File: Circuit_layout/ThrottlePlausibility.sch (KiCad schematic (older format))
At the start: 65 parts, among them Q2 MMBF170, SW2 TS5A3159-Q1, U18 TS912, U22 TS372, U23 TLP293, U24 TLP293, U3 MCP6004, U4 MCP6004, U5 LM7810CT, U6 TS912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

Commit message: fixing nets. most done except for GND/driving issue
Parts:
- W10, W11, W6, W7, W8: footprint (none) -> Measurement_Points:Measurement_Point_Round-SMD-Pad_Big
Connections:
- net VCC is gone; now on net +5V: U8.11 (VCC)

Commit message: current sensor enable
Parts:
- W4, W5: footprint (none) -> Measurement_Points:Measurement_Point_Round-SMD-Pad_Big

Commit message: modifying hvpl
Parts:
- U5: footprint TO-220 -> Power_Integrations:TO-220
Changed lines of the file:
@@
 LIBS:xilinx
 LIBS:Zilog
-LIBS:pacman-main-cache
 LIBS:bss84
 LIBS:+10v
@@
 F 0 "JP1" H 13700 4600 50  0000 L CNN
 F 1 "JUMPER3" H 13650 4800 50  0000 C BNN
-F 2 "" H 13650 4700 50  0000 C CNN
+F 2 "" H 13650 4700 50  0001 C CNN
 F 3 "" H 13650 4700 50  0000 C CNN
 	1    13650 4700
@@
 F 0 "U5" H 1800 4300 50  0000 C CNN
 F 1 "LM7810CT" H 2000 4300 50  0000 L CNN
-F 2 "TO-220" H 2000 4200 50  0001 C CIN
+F 2 "Power_Integrations:TO-220" H 2000 4200 50  0001 C CIN
 F 3 "https://www.fairchildsemi.com/datasheets/LM/LM7805.pdf" H 2000 4100 50  0001 C CNN
 F 4 "LM7810CT-ND" H 2000 4100 60  0001 C CNN "DigiKey P/N"
@@
 F 0 "W9" H 11550 4970 50  0000 C CNN
 F 1 "Throttle_PL" H 11550 4900 50  0000 C CNN
-F 2 "" H 11750 4700 50  0000 C CNN
+F 2 "" H 11750 4700 50  0001 C CNN
 F 3 "" H 11750 4700 50  0000 C CNN
 	1    11550 4700

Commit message: added footprint to DPDT switch, test points, DRC passes
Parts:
- renumbered U6 to U18, U18 to U6
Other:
- moved on the sheet: C45

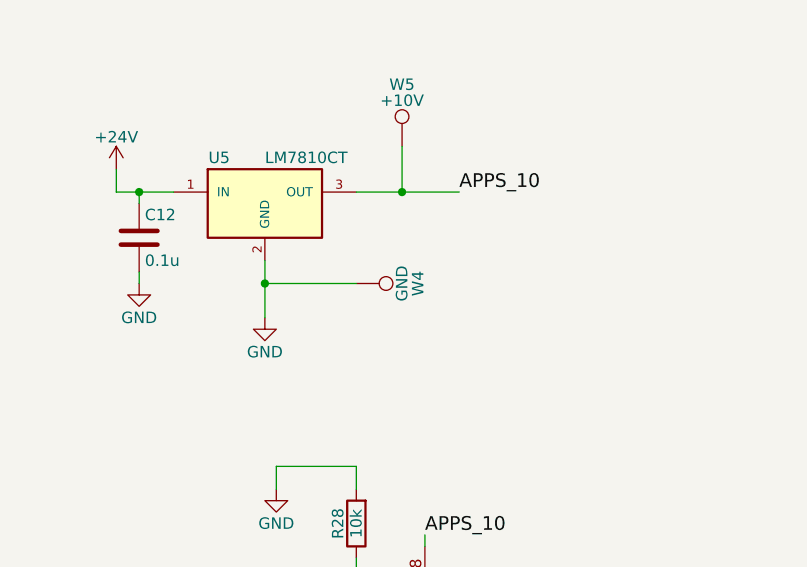
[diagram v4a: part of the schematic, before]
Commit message: cleaned up footprints of more testpoints. ran DRC again, passed
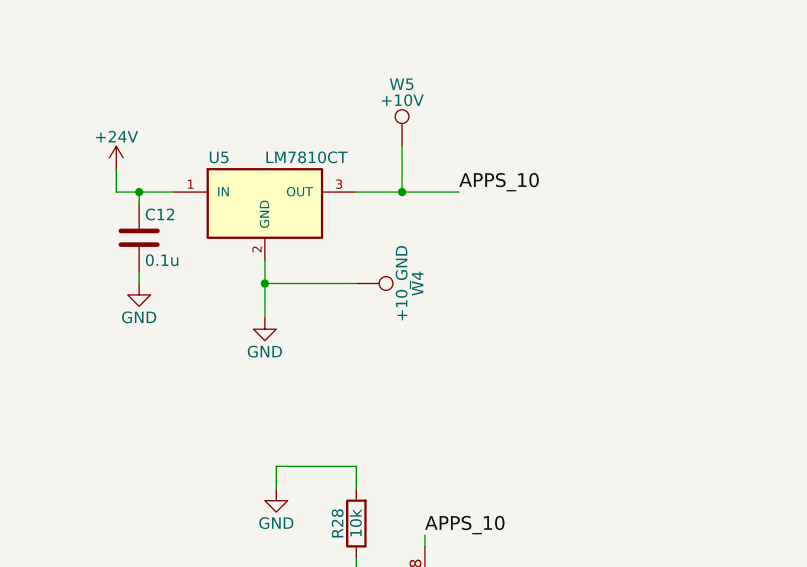
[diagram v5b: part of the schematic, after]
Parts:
- W4: value GND -> +10_GND; footprint Measurement_Points:Measurement_Point_Round-SMD-Pad_Big -> Measurement_Points:Measurement_Point_Square-SMD-Pad_Big

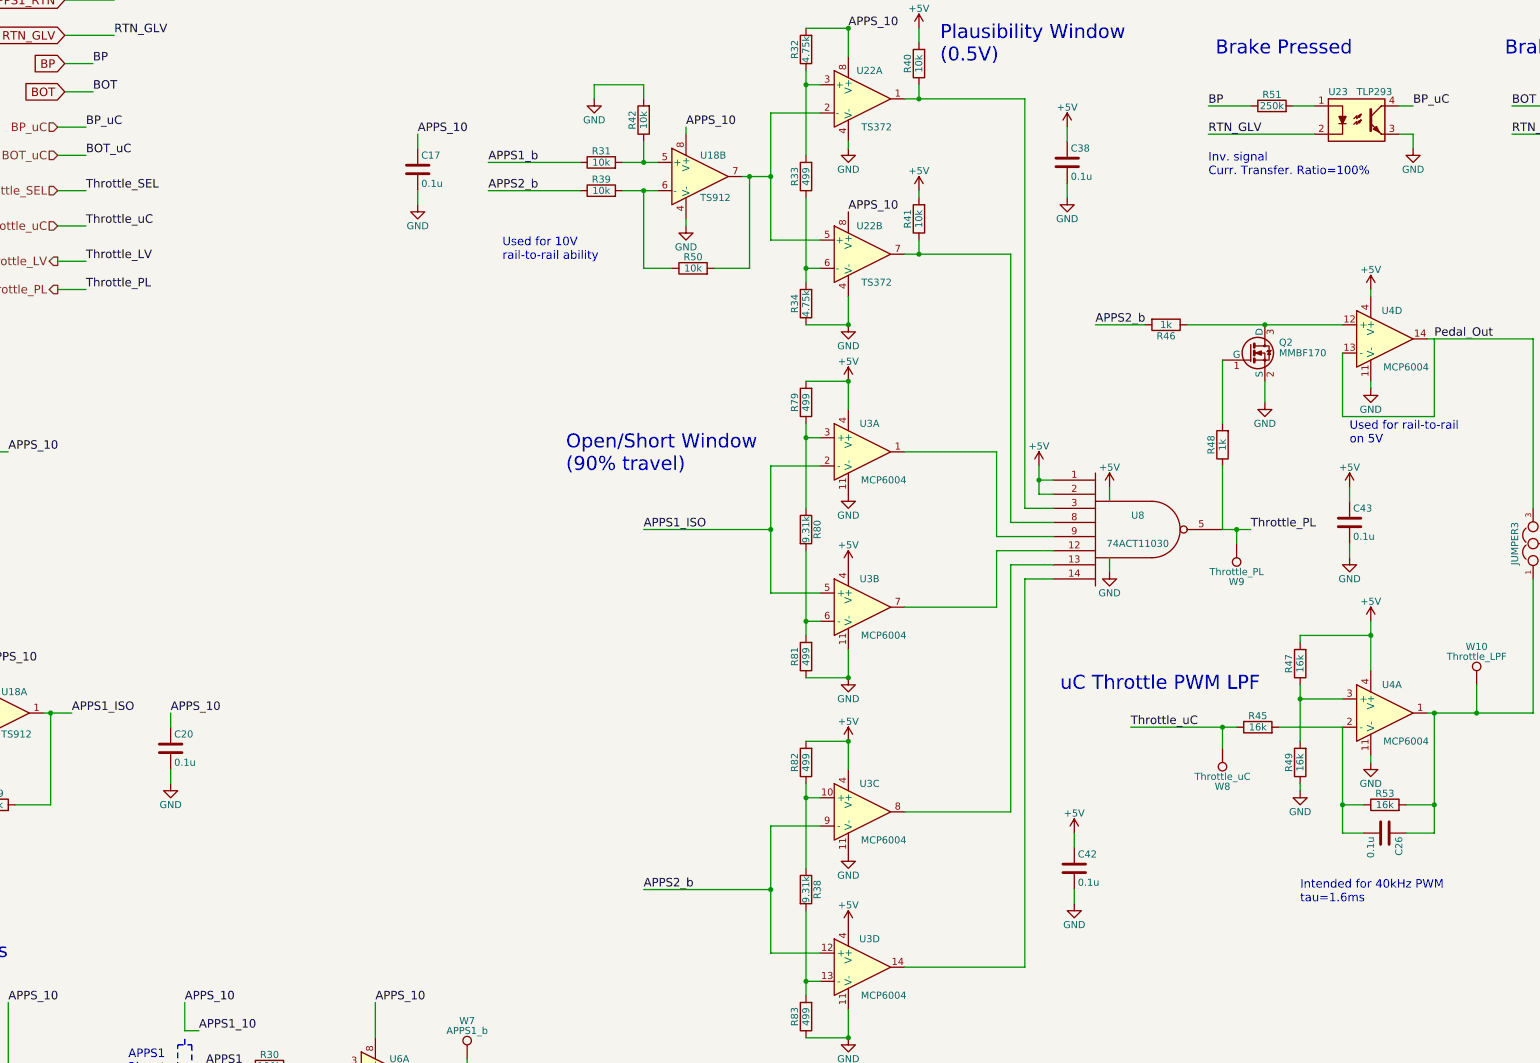
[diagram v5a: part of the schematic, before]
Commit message: started working on throttle layout in pcb. added ch_gnd plane
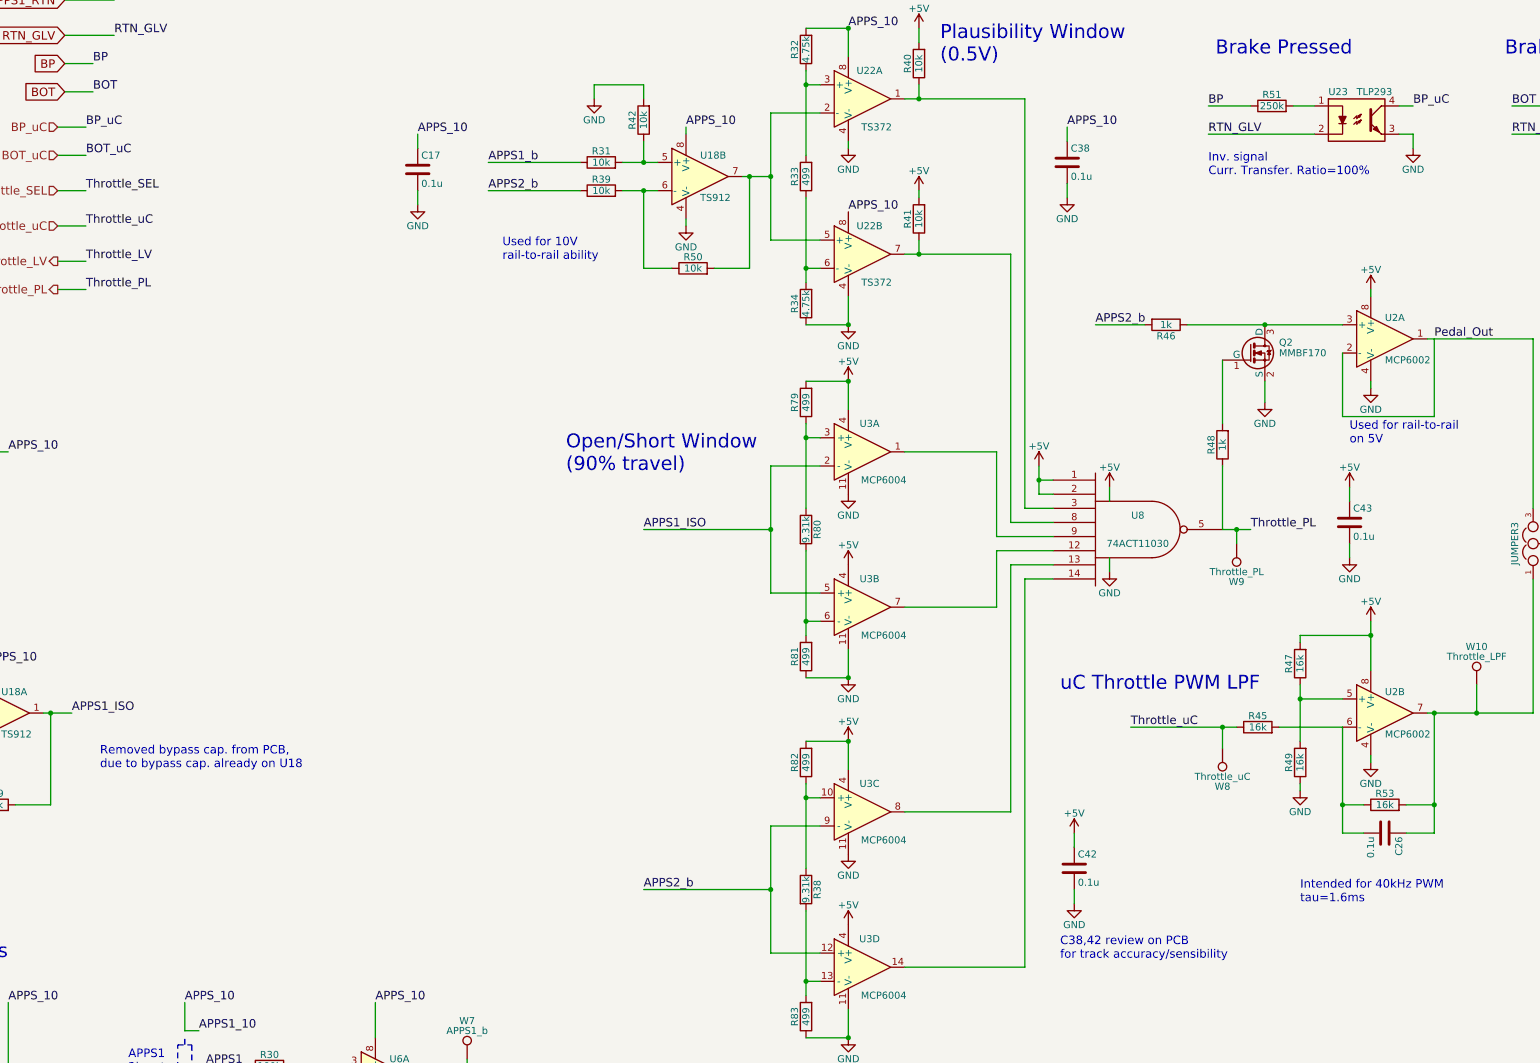
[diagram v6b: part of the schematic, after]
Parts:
- removed C20: 0.1u, Capacitors_SMD:C_0805_HandSoldering, symbol C
- removed U4: MCP6004, Housings_SOIC:SOIC-14_3.9x8.7mm_Pitch1.27mm, symbol MCP6004
- added U2: MCP6002, Housings_SOIC:SOIC-8_3.9x4.9mm_Pitch1.27mm, symbol MCP6002
- JP1: footprint (none) -> Pin_Headers:Pin_Header_Straight_1x03_Pitch2.54mm; Cost (none) -> 0.26; Description (none) -> JUMPER PLUG 3POS SING ROW; DigiKey P/N (none) -> Z5375-ND; Man P/N (none) -> XG8V-0331; URL (none) -> http://www.digikey.com/product-detail/en/omron-electronics-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
- W9: footprint (none) -> Measurement_Points:Measurement_Point_Round-SMD-Pad_Big
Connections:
- net +5V: now also U2.8 (V+), U2.8 (V+); no longer C38.1
- net APPS1_10: now also C38.1
- net GND: now also U2.4 (V-), U2.4 (V-)
- net Pedal_Out: now also U2.1, U2.2 (-)
- net at Q2.3 (D), R46.1: now also U2.3 (+)
- net at C26.1, JP1.1, R53.2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: now also U2.7
- net at C26.2, R45.2, R53.1: now also U2.6 (-)
- net at R47.1, R49.2: now also U2.5 (+)
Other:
- note added: "C38,42 review on PCB\nfor track accuracy/sensibility"
- note added: "Removed bypass cap. from PCB, \ndue to bypass cap. already on U18"

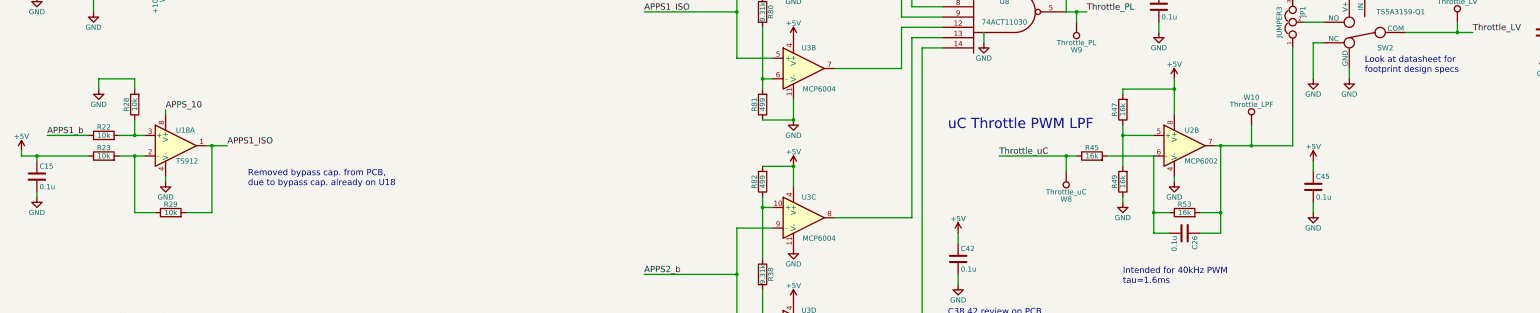
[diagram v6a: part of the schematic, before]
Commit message: reviewed schematic w/ prof. nadovich. proposed changes
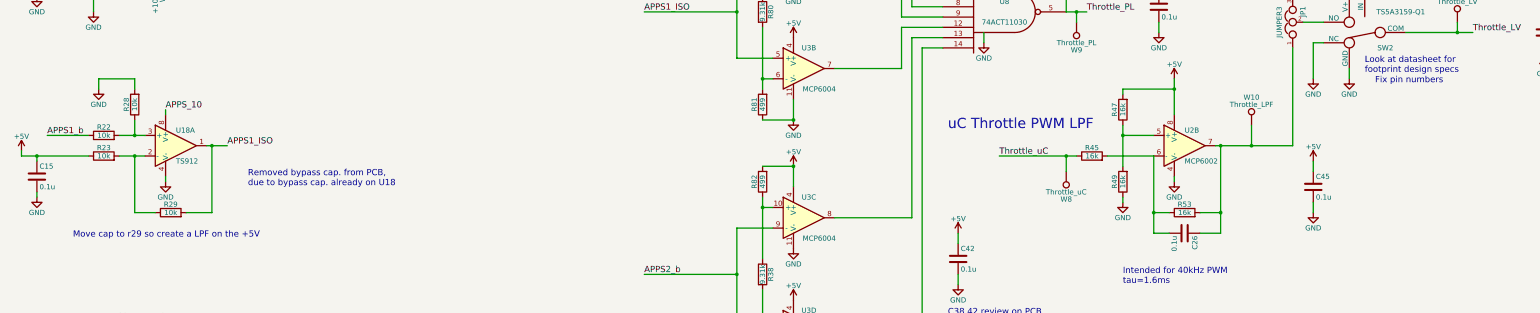
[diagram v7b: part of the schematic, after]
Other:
- note added: "Fix pin numbers"
- note added: "Move cap to r29 so create a LPF on the +5V"
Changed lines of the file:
@@
 Text Label 10350 1750 0    60   ~ 0
 APPS_10
+Text Notes 14450 5300 0    60   ~ 0
+Fix pin numbers
+Text Notes 1800 6800 0    60   ~ 0
+Move cap to r29 so create a LPF on the +5V
 $EndSCHEMATC
